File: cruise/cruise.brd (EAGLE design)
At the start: 100 x 80 mm, 26 parts, among them IC1 24C04ASM, U1 STM32F103CBT6

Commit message: работа над схемой
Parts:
- removed T3: (no value), transistor:SOT23-BEC
- added C10, C9: 20pf, rcl:C0805
- added C11, C12, C14, C16, C17, C18, C19: 100nf, rcl:C0805
- added C13: 1uF, rcl:C0805
- added C15: 10uF, rcl:C0805
- added C5, C7: 10uF, rcl:CT6032
- added C6, C8: 1uF, rcl:CT6032
- added D1, D2: 5.1V, diode:SOD80C
- added D3, D5, D6: 3V3, diode:SOD80C
- added D4: 3v3, diode:SOD80C
- added D7, D8: 3.3V, diode:SOD80C
- added J1: (no value), jumper:04C
- added M0, M1, PAD1, PAD2, PAD3, PAD4, PAD5: (no value), wirepad:2,54/1,0
- added Q1, Q2, Q3: BSS138, m-pad-2.1:SOT23
- added Q4: 8MHz, crystal:SM49
- added R18: 200, resistor:R0805
- added R19: 1.5K, resistor:R0805
- added R20, R22, R23, R24, R27: 10K, resistor:R0805
- added R21: 6.8K, resistor:R0805
- added R25, R26: 4.7K, resistor:R0805
- added S1: (no value), m-pad-2.1:EVQ-PJU05K
- added X1: (no value), Rembrandt Electronics - JST XH Connectors v1-0:JST-XH-02-PACKAGE-LONG-PAD
- added X2: JST-XH-04-PIN-LONG-PAD, Rembrandt Electronics - JST XH Connectors v1-0:JST-XH-04-PACKAGE-LONG-PAD
- added X3: (no value), Rembrandt Electronics - JST XH Connectors v1-0:JST-XH-05-PACKAGE-LONG-PAD
- added X4: (no value), Rembrandt Electronics - JST XH Connectors v1-0:JST-XH-06-PACKAGE-LONG-PAD
- C1: value 1nf -> 1nF; device rcl:C1206 -> rcl:C0805
- C2: value 10uf -> 1nF; device rcl:B/3528-21W -> rcl:C0805
- C3: value 1nf -> 5uF; device rcl:C1206 -> rcl:CT6032
- C4: value 10uf -> 10uF; device rcl:B/3528-21W -> rcl:CT6032
- R1, R14: value 10k -> 10K
- R10, R2: value 6.8k -> 10K
- R11, R13, R7, R9: value 10k -> 3.3K
- R12, R16: value 4.7k -> 10K
- R15: value 10k -> 6.8K
- R17: value 4.7k -> 6.8K
- R3, R5: value 10k -> 4.7K
- R4: value 6.8k -> 4.7K
- R6, R8: value 3.3k -> 10K
- T1, T2: device transistor:SOT23-BEC -> transistor-neu-to92:SOT23-BEC
- moved R15 82.7 mm to (10.2, 33.0)
- moved R16 58.5 mm to (26.7, 15.2), turned to 270 degrees
- moved R9 56.6 mm to (44.5, 16.5), turned to 90 degrees
- moved R17 55.7 mm to (26.7, 10.2), turned to 270 degrees
- moved R14 49.9 mm to (10.2, 35.6), turned to 180 degrees
- moved R12 46.7 mm to (52.1, 8.89), turned to 270 degrees
- moved C1 43.2 mm to (68.6, 8.89), turned to 90 degrees
- moved R1 39.6 mm to (73.7, 8.89), turned to 90 degrees
- moved R7 36.1 mm to (80.0, 20.3), turned to 180 degrees
- moved C3 35.3 mm to (59.7, 20.3), turned to 180 degrees
- moved R10 33.9 mm to (83.8, 8.89), turned to 90 degrees
- moved U1 33.8 mm to (45.7, 39.4)
- moved T1 33.0 mm to (73.7, 21.6)
- moved C2 32.5 mm to (71.1, 8.89), turned to 90 degrees
- moved R13 31.2 mm to (52.1, 14.0), turned to 90 degrees
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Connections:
- net SWDCLK renamed N$40
- net SWDIO renamed N$39
- net USART_RX renamed N$36
- net USART_TX renamed N$34
- net USB_CTS renamed N$37
- net USB_RTS renamed N$38
- removed net I2C_SCL: U1.42
- removed net I2C_SDA: U1.43
- removed net STOP_EXTI3: R14.1, R7.1, R8.2, T2.B, T2.C, U1.13
- removed net VDDA: U1.9
- removed net VDD_2: U1.36
- removed net VDD_3: U1.48
- removed net VNH2_SP30_CS_IN: R9.2
- new net +12V: X2.3, X3.3
- new net BOOT0: R27.1, U1.44
- new net CRUISE_LAMP_OUT_PB15: Q1.1, R22.1, U1.28
- new net D_IN: C7.+, R12.2, X3.2
- new net D_IN_PA8: D4.C, R12.1, R13.1, U1.29
- new net IDLE_IN: C6.+, R10.1, X4.5
- new net IDLE_IN_PB14: D6.C, R10.2, R11.2, U1.27
- new net M0: M0.1, X2.1
- new net M1: M1.1, X2.2
- new net N$15: R16.2, R17.1
- new net N$18: U1.41
- new net N$2: C9.1, Q4.2, U1.5
- new net N$20: U1.39
- new net N$25: U1.11
- new net N$26: U1.12
- new net N$28: U1.14
- new net N$29: U1.16
- new net N$3: C10.2, Q4.1, U1.6
- new net N$30: U1.15
- new net N$32: Q1.3, X3.4
- new net N$35: Q2.3, X3.5
- new net N$4: D1.C, R2.2, R5.1, T2.B
- new net N$41: U1.38
- new net N$6: D2.C, R1.2, T1.B
- new net N$7: J1.2, R27.2
- new net N$9: C11.1, S1.2
- new net OD_IN_L: C5.+, R8.2, X3.1
- new net OD_IN_LIGHT_PB12: D5.C, R8.1, R9.1, U1.25
- new net OD_OUT_BUTTON_PB13: Q2.1, R23.1, U1.26
- new net RST: C11.2, S1.1, U1.7
- new net STOP_IN_PA3: D3.C, R6.2, R7.2, U1.13
- new net SW_IN: C8.+, R18.1, X1.2
- net GND: now also C10.1, C12.1, C13.1, C14.1, C15.1, C16.1, C17.1, C18.1, C19.1, C2.2, C3.-, C5.-, C6.-, C7.-, C8.-, C9.2, D1.A, D2.A, D3.A, D4.A, D5.A, D6.A, D7.A, D8.A, J1.1, Q1.2, Q2.2, Q3.2, R11.1, R13.2, R15.2, R17.2, R21.2, R22.2, R23.2, R24.2, R5.2, R7.1, R9.2, X1.1, X4.6; no longer C2.-, C3.2, R10.1, R12.1, R2.1, R4.1, R6.1, R8.1, T3.E
- net N$1: now also Q3.3, X2.4; no longer R11.1, R12.2, T1.B
- net PB2_OUT_SOLENOID: now also Q3.1, R24.1, U1.20; no longer U1.29
- net RPM_EXTI11: now also R4.1, T2.C; no longer R13.1, T1.C
- net RPM_IN: now also R2.1, X4.2; no longer R11.2
- net SCL: now also R25.2, U1.42; no longer R16.1
- net SDA: now also R26.2, U1.43; no longer R17.1
- net SPD_IN: now also C2.1, R1.1, X4.3; no longer C3.1, R5.2
- net STOP_IN: now also C4.+, R6.1, X4.4; no longer C2.+, R7.2
- net SWITCH_ADC: now also D7.C, R18.2, R19.1
- net TIM3_CH2_SPD: now also R3.1, T1.C; no longer R15.1, R5.1, R6.2, T3.B, T3.C
- net TPS_ADC: now also C3.+, D8.C, R20.2, R21.1; no longer R1.1, R2.2
- net TPS_IN: now also R20.1, X4.1; no longer C4.+, R1.2
- net VCC: now also C12.2, C13.2, C14.2, C15.2, C16.2, C17.2, C18.2, C19.2, J1.3, R19.2, R25.1, R26.1, R3.2, R4.2, U1.24, U1.36, U1.48, U1.9; no longer R13.2, R14.2, R15.2, R16.2, R17.2
- net VNH2_SP30_CS: now also PAD4.1, R16.1; no longer R10.2, R9.1
- net VNH2_SP30_EN: now also PAD3.1, R14.2, R15.1; no longer R3.1, R4.2
- net VNH2_SP30_EN_IN: now also R14.1; no longer R3.2
- net VNH2_SP30_INA: now also PAD1.1
- net VNH2_SP30_INB: now also PAD2.1
- net VNH2_SP30_PWM: now also PAD5.1
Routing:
- net SWITCH_ADC: track 0.00 -> 36.1 mm
- net D_IN_PA8: track 0.00 -> 30.9 mm
- net RST: track 0.00 -> 30.2 mm
- net OD_IN_LIGHT_PB12: track 0.00 -> 29.4 mm
- net OD_IN_L: track 0.00 -> 19.4 mm
- net N$1: track 0.00 -> 18.5 mm
- net TPS_ADC: track 0.00 -> 18.1 mm
- net IDLE_IN: track 0.00 -> 15.3 mm
- net N$3: track 0.00 -> 13.7 mm
- net N$4: track 0.00 -> 13.7 mm
- net N$2: track 0.00 -> 13.5 mm
- net SW_IN: track 0.00 -> 12.0 mm
- net N$6: track 0.00 -> 11.7 mm
- net STOP_IN_PA3: track 0.00 -> 11.7 mm
- net STOP_IN: track 0.00 -> 11.2 mm
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- added copper zone on layer 1, net GND

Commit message: работа над схемой
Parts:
- removed PAD1, PAD2, PAD3, PAD4, PAD5: (no value), wirepad:2,54/1,0
- added CS, EN, INA, INB, PWM: (no value), wirepad:2,54/1,0
- added IC2: 7805T, linear:TO220H
- added IC3: LD117AS33TR, v-reg:SOT223
- added Q5, Q6, Q7: BSS138, m-pad-2.1:SOT23
- added R28, R29, R30, R32, R33: 10K, resistor:R0805
- added R31: 510, resistor:R0805
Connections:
- removed net N$15: R16.2, R17.1
- new net +5V: IC2.3, IC3.3, R31.1, R32.1, R33.1
- new net N$10: INA.1, Q5.3, R33.2
- new net N$5: PWM.1, Q7.3, R31.2
- new net N$8: INB.1, Q6.3, R32.2
- new net VNH2_SP30_CS_IN: CS.1, R16.1
- net +12V: now also IC2.1
- net GND: now also IC2.2, IC3.1
- net VCC: now also IC3.4, Q5.1, Q6.1, Q7.1, R28.2, R29.1, R30.2
- net VNH2_SP30_CS: now also R16.2, R17.1; no longer PAD4.1, R16.1
- net VNH2_SP30_EN: no longer PAD3.1
- net VNH2_SP30_EN_IN: now also EN.1
- net VNH2_SP30_INA: now also Q5.2, R30.1; no longer PAD1.1
- net VNH2_SP30_INB: now also Q6.2, R28.1; no longer PAD2.1
- net VNH2_SP30_PWM: now also Q7.2, R29.2; no longer PAD5.1
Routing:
- net VNH2_SP30_EN: track 6.67 -> 2.54 mm

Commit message: схема
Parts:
- added +12V4A, +5V, GND: (no value), wirepad:2,54/1,0
- added ARMED, D_IN, IDLE, OD_IN, OD_OUT, RPM, SL, SPD, STOP, VCC: (no value), led:CHIP-LED0805
- added C20: 470uF, rcl:PANASONIC_G
- added C21, C23, C25: 100nf, rcl:C0805
- added C22, C24: 220uF, rcl:CT6032
- added F1: 500mA, m-pad-2.1:1206
- added F2: 2000mA, m-pad-2.1:1206
- added F3: 4000mA, m-pad-2.1:1206
- added JP1: (no value), jumper:JP10Q
- added R34, R35: 200, resistor:R0805
- added R36, R37, R38, R39, R40, R41, R42, R43, R44, R45: 510, resistor:R0805
- added U$1: (no value), my:DFN450X400X350-2
- added U$2, U$3, U$4, U$5: (no value), holes:3,2
- added X5: SWD, Rembrandt Electronics - JST XH Connectors v1-0:JST-XH-06-PACKAGE-LONG-PAD
- added X6: I2C, Rembrandt Electronics - JST XH Connectors v1-0:JST-XH-04-PACKAGE-LONG-PAD
- added X7: JST-XH-06-PIN-LONG-PAD, Rembrandt Electronics - JST XH Connectors v1-0:JST-XH-06-PACKAGE-LONG-PAD
- C1, C10, C11, C12, C13, C14, C15, C16, C17, C18, C19, C2, C9: device rcl:C0805 -> rcl:C0805K
- C3: value 5uF -> 100nf; device rcl:CT6032 -> rcl:C0805K
- C4, C5, C7: value 10uF -> 100nf; device rcl:CT6032 -> rcl:C0805K
- C6, C8: value 1uF -> 100nf; device rcl:CT6032 -> rcl:C0805K
- Q4: device crystal:SM49 -> crystal-geyer_V1_0:5.0X3.2_2
- moved IC3 73.1 mm to (19.1, 58.4), flipped to the bottom
- moved IC2 63.6 mm to (26.7, 71.1)
- moved R10 57.4 mm to (66.0, 63.5), flipped to the bottom
- moved C6 55.4 mm to (68.6, 63.5), flipped to the bottom
- moved D6 50.0 mm to (66.0, 63.5), turned to 270 degrees
- moved X4 49.6 mm to (73.7, 52.1), turned to 90 degrees
- moved R6 49.3 mm to (66.0, 57.1), flipped to the bottom
- moved Q5 48.7 mm to (18.2, 25.0), turned to 270 degrees
- moved C4 47.1 mm to (68.6, 57.1), flipped to the bottom
- moved R11 46.7 mm to (68.6, 63.5), turned to 90 degrees
- moved X1 45.0 mm to (73.7, 15.2), turned to 90 degrees
- moved IC1 44.4 mm to (36.8, 61.0), turned to 0 degrees
- moved R1 43.8 mm to (66.0, 52.1), flipped to the bottom, turned to 270 degrees
- moved C2 43.3 mm to (68.6, 52.1), flipped to the bottom, turned to 270 degrees
- moved R25 43.1 mm to (35.6, 67.3)
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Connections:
- new net +12V2A: F2.2
- new net +12V4A: +12V4A.1, F3.2, X2.3
- new net +12V_FUSED: C20.+, C21.2, IC2.1, U$1.2
- new net N$11: R34.1, X6.3
- new net N$12: R35.1, X6.4
- new net N$13: F1.2, U$1.1
- new net N$14: JP1.20, R36.2
- new net N$15: R36.1, RPM.A
- new net N$16: R37.1, SPD.A
- new net N$17: R38.1, STOP.A
- new net N$19: OD_IN.A, R39.1
- new net N$21: D_IN.A, R40.1
- new net N$22: IDLE.A, R41.1
- new net N$23: R42.1, VCC.A
- new net N$24: ARMED.A, R43.1
- new net N$27: JP1.18, R37.2
- new net N$31: JP1.16, R38.2
- new net N$33: JP1.14, R39.2
- new net N$42: JP1.8, R42.2
- new net N$43: JP1.6, R43.2
- new net N$44: OD_OUT.A, R44.1
- new net N$45: R45.1, SL.A
- new net N$46: JP1.4, R44.2
- new net N$47: JP1.2, R45.2
- new net SWDCLK: U1.37, X5.4
- new net SWDIO: U1.34, X5.3
- net +12V: now also F1.1, F2.1, F3.1, X7.4, X7.5, X7.6; no longer IC2.1, X2.3, X3.3
- net +5V: now also +5V.1, C22.+, C23.2
- net CRUISE_LAMP_OUT_PB15: now also JP1.7
- net D_IN: now also C7.1; no longer C7.+
- net D_IN_PA8: now also JP1.5
- net GND: now also ARMED.C, C20.-, C21.1, C22.-, C23.1, C24.-, C25.1, C3.2, C4.2, C5.2, C6.2, C7.2, C8.2, D_IN.C, GND.1, IDLE.C, OD_IN.C, OD_OUT.C, RPM.C, SL.C, SPD.C, STOP.C, U1.23, U1.35, U1.47, U1.8, VCC.C, X5.1, X6.1, X7.1, X7.2, X7.3; no longer C3.-, C4.-, C5.-, C6.-, C7.-, C8.-
- net IDLE_IN: now also C6.1; no longer C6.+
- net IDLE_IN_PB14: now also JP1.9
- net N$39: now also JP1.12, R40.2; no longer U1.34
- net N$40: now also JP1.10, R41.2; no longer U1.37
- net OD_IN_L: now also C5.1; no longer C5.+
- net OD_IN_LIGHT_PB12: now also JP1.13
- net OD_OUT_BUTTON_PB13: now also JP1.11
- net PB2_OUT_SOLENOID: now also JP1.17
- net RPM_EXTI11: now also JP1.15
- net SCL: now also R35.2
- net SDA: now also R34.2
- net STOP_IN: now also C4.1; no longer C4.+
- net STOP_IN_PA3: now also JP1.19
- net SW_IN: now also C8.1; no longer C8.+
- net TIM3_CH2_SPD: now also JP1.1
- net TPS_ADC: now also C3.1; no longer C3.+
- net VCC: now also C24.+, C25.2, JP1.3, X5.2, X6.2
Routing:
- net VCC: track 0.00 -> 294.2 mm, vias 0 -> 9
- net +5V: track 0.00 -> 79.9 mm
- net STOP_IN_PA3: track 11.7 -> 75.0 mm, vias 0 -> 5
- net IDLE_IN_PB14: track 11.1 -> 73.0 mm, vias 0 -> 4
- net +12V4A: track 0.00 -> 58.5 mm
- net GND: track 3.18 -> 59.4 mm, vias 0 -> 6
- net SWDIO: track 0.00 -> 49.4 mm, vias 0 -> 3
- net PB2_OUT_SOLENOID: track 4.59 -> 49.8 mm
- net RPM_EXTI11: track 0.00 -> 45.0 mm, vias 0 -> 3
- net OD_OUT_BUTTON_PB13: track 3.06 -> 47.4 mm, vias 0 -> 4
- net TIM3_CH2_SPD: track 3.03 -> 46.6 mm, vias 0 -> 5
- net CRUISE_LAMP_OUT_PB15: track 3.06 -> 46.3 mm, vias 0 -> 3
- net SWDCLK: track 0.00 -> 41.8 mm, vias 0 -> 3
- net VNH2_SP30_INA: track 0.00 -> 40.9 mm
- net VNH2_SP30_INB: track 0.00 -> 38.4 mm
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- added copper zone on layer 16, net GND
- added copper zone on layer 16, net NC
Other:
- board size 100 x 80 mm -> 75.2 x 80 mm

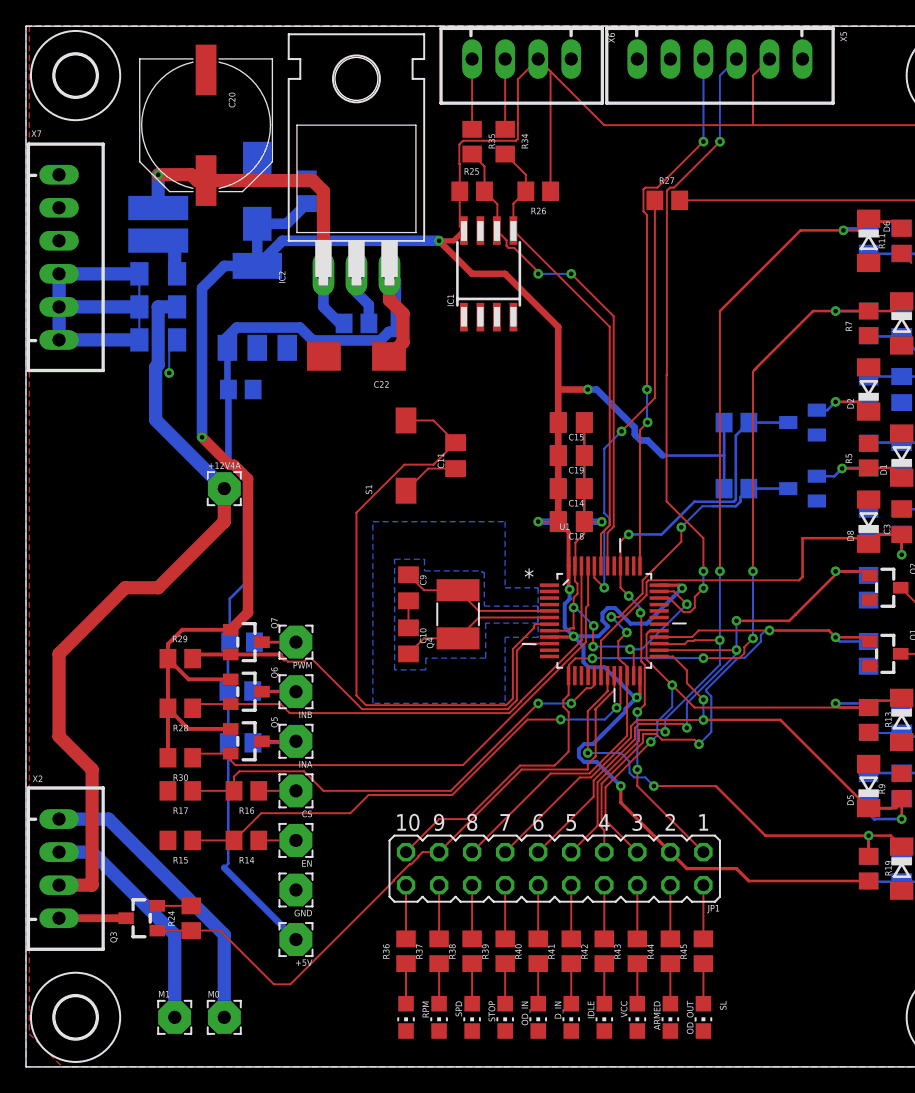
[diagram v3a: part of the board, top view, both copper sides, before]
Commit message: схема+проверка работы мотора
какой то косяк с шимом. Наверное зря удалил подтягивающий резистор. Нормально работает только на частоте до 1кгц
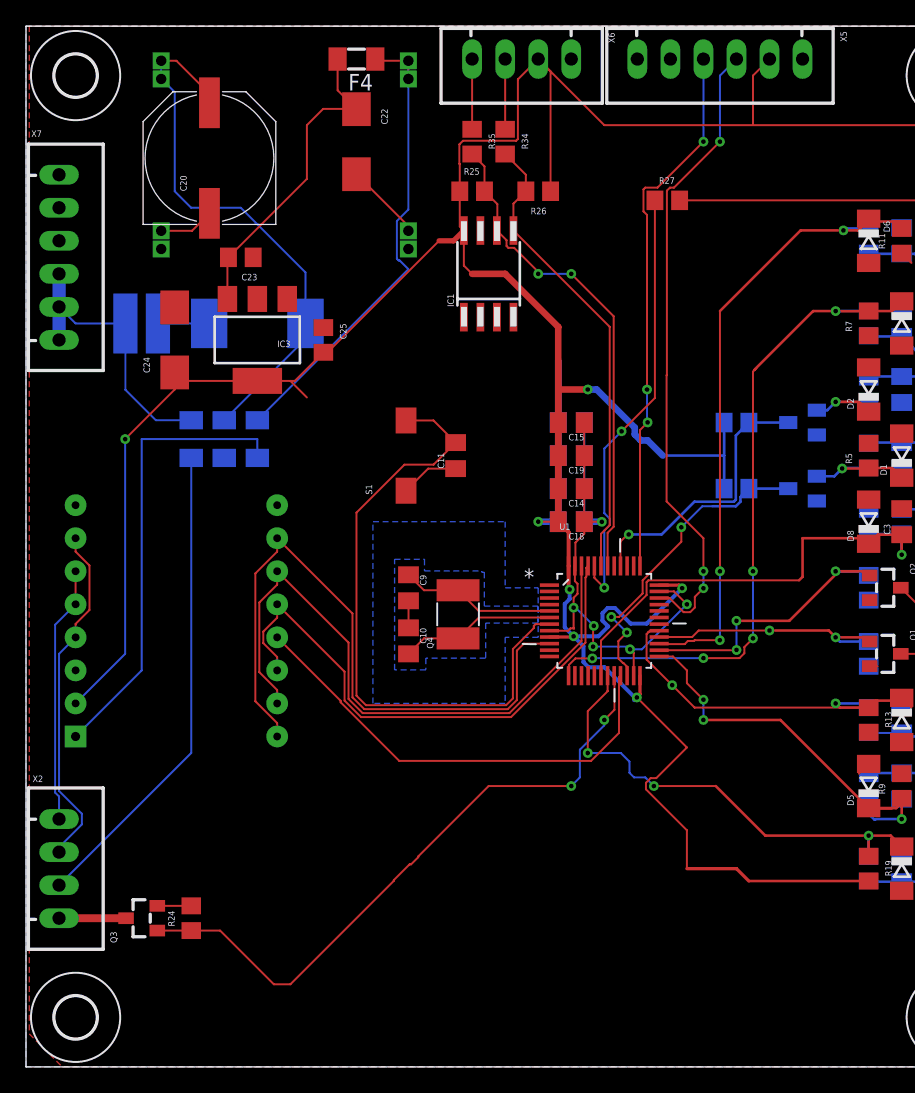
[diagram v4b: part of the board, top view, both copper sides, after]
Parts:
- removed +12V4A, +5V, CS, EN, GND, INA, INB, M0, M1, PWM: (no value), wirepad:2,54/1,0
- removed ARMED, D_IN, IDLE, OD_IN, OD_OUT, RPM, SL, SPD, STOP, VCC: (no value), led:CHIP-LED0805
- removed C21: 100nf, rcl:C0805
- removed IC2: 7805T, linear:TO220H
- removed JP1: (no value), jumper:JP10Q
- removed Q5, Q6, Q7: BSS138, m-pad-2.1:SOT23
- removed R14, R16, R28, R29, R30, R32, R33: 10K, resistor:R0805
- removed R15, R17: 6.8K, resistor:R0805
- removed R31, R36, R37, R38, R39, R40, R41, R42, R43, R44, R45: 510, resistor:R0805
- added D9: (no value), eagle-ltspice:DIODE_SMC
- added F4: 500mA, m-pad-2.1:1206
- added TB1: TB6612FNG, TB6612FNG:TB6612FNG
- added U$6: MP1584, MP1584-dc-brick:DC-BRICK
- F3: value 4000mA -> 2000mA
- moved C22 16.5 mm to (26.7, 71.1), turned to 270 degrees
- moved F1 13.7 mm to (16.5, 48.3), turned to 270 degrees
- moved C24 13.1 mm to (12.7, 55.9), flipped to the top
- moved F3 12.7 mm to (19.1, 48.3), turned to 270 degrees
- moved C25 11.5 mm to (24.1, 55.9), flipped to the top
- moved C23 10.2 mm to (17.8, 62.2), flipped to the top, turned to 180 degrees
- moved F2 8.03 mm to (14.0, 48.3), turned to 270 degrees
- moved U$1 7.73 mm to (10.2, 57.1), turned to 180 degrees
- moved IC3 2.54 mm to (19.1, 55.9), flipped to the top, turned to 180 degrees
- moved C20 2.53 mm to (15.4, 69.9), turned to 90 degrees
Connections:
- removed net +12V2A: F2.2
- removed net +12V4A: +12V4A.1, F3.2, X2.3
- removed net +12V_FUSED: C20.+, C21.2, IC2.1, U$1.2
- removed net N$10: INA.1, Q5.3, R33.2
- removed net N$14: JP1.20, R36.2
- removed net N$15: R36.1, RPM.A
- removed net N$16: R37.1, SPD.A
- removed net N$17: R38.1, STOP.A
- removed net N$19: OD_IN.A, R39.1
- removed net N$21: D_IN.A, R40.1
- removed net N$23: R42.1, VCC.A
- removed net N$24: ARMED.A, R43.1
- removed net N$27: JP1.18, R37.2
- removed net N$31: JP1.16, R38.2
- removed net N$33: JP1.14, R39.2
- removed net N$39: JP1.12, R40.2
- removed net N$40: JP1.10, R41.2
- removed net N$42: JP1.8, R42.2
- removed net N$43: JP1.6, R43.2
- removed net N$44: OD_OUT.A, R44.1
- removed net N$45: R45.1, SL.A
- removed net N$46: JP1.4, R44.2
- removed net N$47: JP1.2, R45.2
- removed net N$8: INB.1, Q6.3, R32.2
- removed net VNH2_SP30_CS: R16.2, R17.1, U1.17
- removed net VNH2_SP30_CS_IN: CS.1, R16.1
- removed net VNH2_SP30_EN_IN: EN.1, R14.1
- new net +12V2A_MOTOR: F3.2, TB1.VM
- new net +12V2A_SOLENOID: F2.2, X2.3
- new net 12V_500MA_SENSORS: F1.2
- net +12V: now also U$1.1; no longer F1.1, F3.1
- net +5V: now also F4.2; no longer +5V.1, IC2.3, R31.1, R32.1, R33.1
- net CRUISE_LAMP_OUT_PB15: no longer JP1.7
- net D_IN_PA8: no longer JP1.5
- net GND: now also TB1.GND1, TB1.GND2, TB1.GND3, U$6.IN1-, U$6.IN2-, U$6.OUT1-, U$6.OUT2-; no longer ARMED.C, C21.1, D_IN.C, GND.1, IC2.2, IDLE.C, OD_IN.C, OD_OUT.C, R15.2, R17.2, RPM.C, SL.C, SPD.C, STOP.C, VCC.C
- net IDLE_IN_PB14: no longer JP1.9
- net M0: now also TB1.A2, TB1.B2; no longer M0.1
- net M1: now also TB1.A1, TB1.B1; no longer M1.1
- net N$13: now also D9.A, U$1.2; no longer F1.2, U$1.1
- net N$22: now also C20.+, D9.C, F1.1, U$6.IN1+, U$6.IN2+; no longer IDLE.A, R41.1
- net N$5: now also F3.1, F4.1, U$6.OUT1+, U$6.OUT2+; no longer PWM.1, Q7.3, R31.2
- net OD_IN_LIGHT_PB12: no longer JP1.13
- net OD_OUT_BUTTON_PB13: no longer JP1.11
- net PB2_OUT_SOLENOID: no longer JP1.17
- net RPM_EXTI11: no longer JP1.15
- net STOP_IN_PA3: no longer JP1.19
- net TIM3_CH2_SPD: no longer JP1.1
- net VCC: now also TB1.VCC; no longer JP1.3, Q5.1, Q6.1, Q7.1, R28.2, R29.1, R30.2
- net VNH2_SP30_EN: now also TB1.STBY; no longer R14.2, R15.1
- net VNH2_SP30_INA: now also TB1.AIN1, TB1.BIN1; no longer Q5.2, R30.1
- net VNH2_SP30_INB: now also TB1.AIN2, TB1.BIN2; no longer Q6.2, R28.1
- net VNH2_SP30_PWM: now also TB1.PWMA, TB1.PWMB; no longer Q7.2, R29.2
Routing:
- net +12V4A: track 58.5 -> 0.00 mm
- net +5V: track 79.9 -> 24.7 mm
- net N$22: track 3.08 -> 42.5 mm
- net +12V2A_SOLENOID: track 0.00 -> 37.0 mm
- net VNH2_SP30_CS: track 36.8 -> 0.00 mm, vias 2 -> 0
- net +12V2A_MOTOR: track 0.00 -> 35.3 mm
- net N$5: track 7.62 -> 37.2 mm
- net +12V_FUSED: track 26.8 -> 0.00 mm, vias 1 -> 0
- net VCC: track 294.2 -> 267.5 mm, vias 9 -> 7
- net CRUISE_LAMP_OUT_PB15: track 46.3 -> 19.7 mm, vias 3 -> 2
- net TIM3_CH2_SPD: track 46.6 -> 21.5 mm, vias 5 -> 1
- net OD_OUT_BUTTON_PB13: track 47.4 -> 23.3 mm, vias 4 -> 3
- net IDLE_IN_PB14: track 73.0 -> 50.6 mm, vias 4 -> 3
- net STOP_IN_PA3: track 75.0 -> 53.1 mm
- net RPM_EXTI11: track 45.0 -> 24.7 mm
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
